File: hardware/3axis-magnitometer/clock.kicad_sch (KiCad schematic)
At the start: 13 parts, among them U1 PCF8563T, Y1 32.768кГц

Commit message: Add files via upload
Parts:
- removed R2, R27, R28, R3: 2.2k, Resistor_SMD:R_0805_2012Metric, symbol Device:R
- removed R4: 10, Resistor_SMD:R_0805_2012Metric, symbol Device:R
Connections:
- net GND: no longer U1.2 (OSCO), Y1.2
- net VCC: now also R1.2
- new net: U1.2 (OSCO), Y1.2
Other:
- moved on the sheet: BT1, C2, C3, D1, R1

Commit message: начата новая трассировка
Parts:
- added C2: 22p, Capacitor_SMD:C_0805_2012Metric, symbol Device:C
- renumbered C2 to C3, C3 to C4
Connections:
- net GND: now also C2.2
- net at U1.2 (OSCO), Y1.2: now also C2.1
- net CLK0: no longer names the net of U1.7 (CLKO)
- net INT: no longer names the net of U1.3 (~{INT})
- no-connect marks 0 -> 2
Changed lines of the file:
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@@
 	(paper "A4")
+	(junction
+		(at 100.33 116.84)
+		(diameter 0)
+		(color 0 0 0 0)
+	)
 	(junction
 		(at 124.46 121.92)
@@
 	)
 	(junction
+		(at 86.36 116.84)
+		(diameter 0)
+		(color 0 0 0 0)
+	)
+	(junction
 		(at 100.33 106.68)
 		(diameter 0)
@@
 		(color 0 0 0 0)
 	)
+	(no_connect
+		(at 147.32 116.84)
+	)
+	(no_connect
+		(at 147.32 114.3)
+	)
 	(wire
 		(pts
@@
 	(wire
 		(pts
+			(xy 86.36 116.84) (xy 86.36 106.68)
+		)
+		(stroke
+			(width 0)
+			(type default)
+		)
+	)
+	(wire
+		(pts
+			(xy 97.79 116.84) (xy 100.33 116.84)
+		)
+		(stroke
+			(width 0)
+			(type default)
+		)
+	)
+	(wire
+		(pts
 			(xy 100.33 115.57) (xy 100.33 116.84)
 		)
@@
 	(wire
 		(pts
-			(xy 86.36 121.92) (xy 86.36 106.68)
+			(xy 86.36 116.84) (xy 90.17 116.84)
+		)
+		(stroke
+			(width 0)
+			(type default)
+		)
+	)
+	(wire
+		(pts
+			(xy 86.36 121.92) (xy 86.36 116.84)
 		)
 		(stroke
@@
 		)
 	)
-	(hierarchical_label "CLK0"
-		(shape output)
-		(at 147.32 114.3 0)
-		(effects
-			(font
-				(size 1.27 1.27)
-			)
-			(justify left)
-		)
-	)
 	(hierarchical_label "SCL"
 		(shape input)
@@
 		)
 	)
-	(hierarchical_label "INT"
-		(shape output)
-		(at 147.32 116.84 0)
-		(effects
-			(font
-				(size 1.27 1.27)
-			)
-			(justify left)
-		)
-	)
 	(hierarchical_label "GND"
 		(shape input)
@@
 			)
 			(justify left)
+		)
+	)
+	(symbol
+		(lib_id "Device:C")
+		(at 93.98 116.84 270)
+		(unit 1)
+		(exclude_from_sim no)
+		(in_bom yes)
+		(on_board yes)
+		(dnp no)
+		(property "Reference" "C2"
+			(at 93.726 110.744 90)
+			(effects
+				(font
+					(size 1.27 1.27)
+				)
+			)
+		)
+		(property "Value" "22p"
+			(at 94.234 112.776 90)
+			(effects
+				(font
+					(size 1.27 1.27)
+				)
+			)
+		)
+		(property "Footprint" "Capacitor_SMD:C_0805_2012Metric"
+			(at 90.17 117.8052 0)
+			(effects
+				(font
+					(size 1.27 1.27)
+				)
+				(hide yes)
+			)
+		)
+		(property "Datasheet" "~"
+			(at 93.98 116.84 0)
+			(effects
+				(font
+					(size 1.27 1.27)
+				)
+				(hide yes)
+			)
+		)
+		(property "Description" "Unpolarized capacitor"
+			(at 93.98 116.84 0)
+			(effects
+				(font
+					(size 1.27 1.27)
+				)
+				(hide yes)
+			)
+		)
+		(pin "1"
+		)
+		(pin "2"
+		)
+		(instances
+			(project "3axis-magnitometer"
+				(path "/c590c88d-27c9-4e5a-a435-a42d9de70c1c/4936c154-a85e-4cc9-be3c-d9a8854356bc"
+					(reference "C2")
+					(unit 1)
+				)
+			)
 		)
 	)
@@
 		(on_board yes)
 		(dnp no)
-		(property "Reference" "C3"
+		(property "Reference" "C4"
 			(at 110.49 92.456 90)
 			(effects
@@
 			(project "3axis-magnitometer"
 				(path "/c590c88d-27c9-4e5a-a435-a42d9de70c1c/4936c154-a85e-4cc9-be3c-d9a8854356bc"
-					(reference "C3")
+					(reference "C4")
 					(unit 1)
 				)
@@
 		(dnp no)
 		(fields_autoplaced yes)
-		(property "Reference" "C2"
+		(property "Reference" "C3"
 			(at 111.379 68.58 90)
 			(effects
@@
 			(project ""
 				(path "/c590c88d-27c9-4e5a-a435-a42d9de70c1c/4936c154-a85e-4cc9-be3c-d9a8854356bc"
-					(reference "C2")
-					(unit 1)
-				)
+					(reference "C3")
+					(unit 1)
+				)

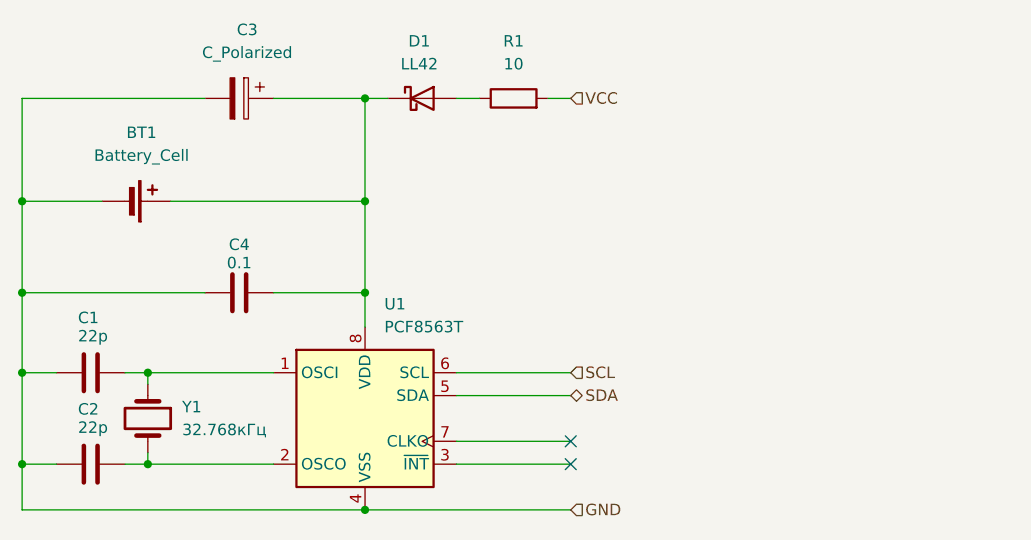
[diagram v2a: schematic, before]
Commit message: Магнитометр правки
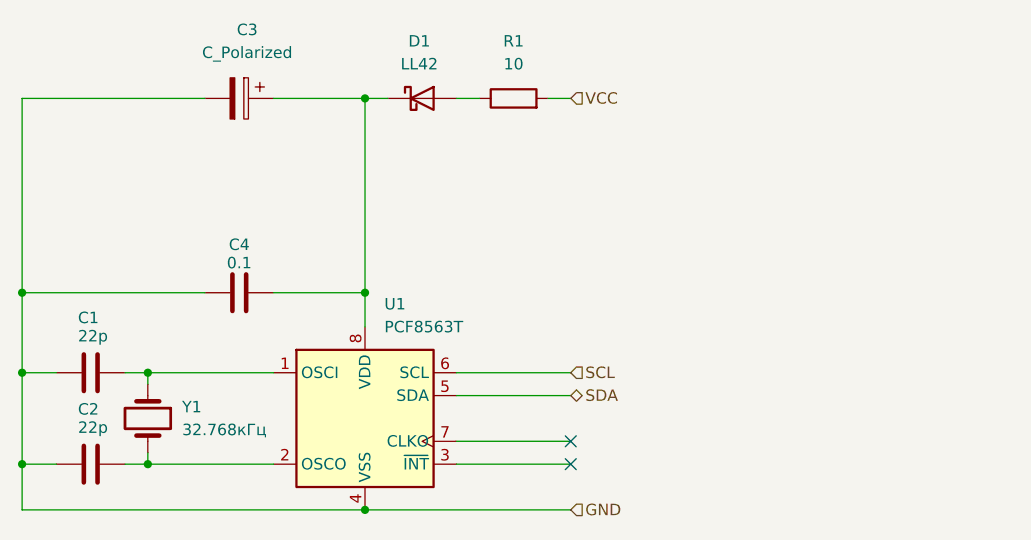
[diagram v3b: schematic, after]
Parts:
- removed BT1: Battery_Cell, Battery:Battery_Panasonic_CR2032-HFN_Horizontal_CircularHoles, symbol Device:Battery_Cell
- C3: footprint Battery:Battery_Panasonic_CR2032-HFN_Horizontal_CircularHoles -> IONISTOR:DSK
- Y1: footprint Crystal:Crystal_SMD_EuroQuartz_EQ161-2Pin_3.2x1.5mm -> Crystal:Crystal_AT310_D3.0mm_L10.0mm_Horizontal_1EP_style2
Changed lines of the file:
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@@
-	)
-	(junction
-		(at 124.46 87.63)
-		(diameter 0)
-		(color 0 0 0 0)
 	)
 	(junction
@@
 	)
 	(junction
-		(at 86.36 87.63)
-		(diameter 0)
-		(color 0 0 0 0)
-	)
-	(junction
 		(at 86.36 106.68)
 		(diameter 0)
@@
 	(wire
 		(pts
-			(xy 86.36 87.63) (xy 86.36 97.79)
+			(xy 86.36 76.2) (xy 86.36 97.79)
 		)
 		(stroke
@@
 	(wire
 		(pts
-			(xy 102.87 87.63) (xy 124.46 87.63)
-		)
-		(stroke
-			(width 0)
-			(type default)
-		)
-	)
-	(wire
-		(pts
 			(xy 124.46 76.2) (xy 127 76.2)
 		)
@@
 	(wire
 		(pts
-			(xy 124.46 76.2) (xy 124.46 87.63)
-		)
-		(stroke
-			(width 0)
-			(type default)
-		)
-	)
-	(wire
-		(pts
 			(xy 144.78 76.2) (xy 147.32 76.2)
 		)
@@
 	(wire
 		(pts
-			(xy 124.46 87.63) (xy 124.46 97.79)
+			(xy 124.46 76.2) (xy 124.46 97.79)
 		)
 		(stroke
@@
 		(pts
 			(xy 134.62 76.2) (xy 137.16 76.2)
-		)
-		(stroke
-			(width 0)
-			(type default)
-		)
-	)
-	(wire
-		(pts
-			(xy 86.36 76.2) (xy 86.36 87.63)
-		)
-		(stroke
-			(width 0)
-			(type default)
-		)
-	)
-	(wire
-		(pts
-			(xy 86.36 87.63) (xy 95.25 87.63)
 		)
 		(stroke
@@
 			)
 		)
-		(property "Footprint" "Crystal:Crystal_SMD_EuroQuartz_EQ161-2Pin_3.2x1.5mm"
+		(property "Footprint" "Crystal:Crystal_AT310_D3.0mm_L10.0mm_Horizontal_1EP_style2"
 			(at 100.33 111.76 0)
 			(effects
@@
 	)
 	(symbol
-		(lib_id "Device:Battery_Cell")
-		(at 97.79 87.63 270)
-		(mirror x)
-		(unit 1)
-		(exclude_from_sim no)
-		(in_bom yes)
-		(on_board yes)
-		(dnp no)
-		(property "Reference" "BT1"
-			(at 99.6315 80.01 90)
-			(effects
-				(font
-					(size 1.27 1.27)
-				)
-			)
-		)
-		(property "Value" "Battery_Cell"
-			(at 99.6315 82.55 90)
-			(effects
-				(font
-					(size 1.27 1.27)
-				)
-			)
-		)
-		(property "Footprint" "Battery:Battery_Panasonic_CR2032-HFN_Horizontal_CircularHoles"
-			(at 99.314 87.63 90)
-			(effects
-				(font
-					(size 1.27 1.27)
-				)
-				(hide yes)
-			)
-		)
-		(property "Datasheet" "~"
-			(at 99.314 87.63 90)
-			(effects
-				(font
-					(size 1.27 1.27)
-				)
-				(hide yes)
-			)
-		)
-		(property "Description" "Single-cell battery"
-			(at 97.79 87.63 0)
-			(effects
-				(font
-					(size 1.27 1.27)
-				)
-				(hide yes)
-			)
-		)
-		(pin "1"
-		)
-		(pin "2"
-		)
-		(instances
-			(project "clock"
-				(path "/051bd5a1-fd18-4bd7-9a14-a1b599706985"
-					(reference "BT?")
-					(unit 1)
-				)
-			)
-			(project ""
-				(path "/c590c88d-27c9-4e5a-a435-a42d9de70c1c/4936c154-a85e-4cc9-be3c-d9a8854356bc"
-					(reference "BT1")
-					(unit 1)
-				)
-			)
-		)
-	)
-	(symbol
 		(lib_id "Device:C_Polarized")
 		(at 110.49 76.2 270)
@@
 			)
 		)
-		(property "Footprint" "Battery:Battery_Panasonic_CR2032-HFN_Horizontal_CircularHoles"
+		(property "Footprint" "IONISTOR:DSK"
 			(at 106.68 77.1652 0)
 			(effects

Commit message: Финальные правки трассировки
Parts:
- added C3: C_Polarized, IONISTOR:DSK, symbol Device:C_Polarized
- renumbered C3 to C4, C4 to C5
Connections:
- net GND: now also C3.2
- net at C4.1, C5.2, D1.1 (K)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: now also C3.1
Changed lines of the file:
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@@
+	)
+	(junction
+		(at 86.36 86.36)
+		(diameter 0)
+		(color 0 0 0 0)
 	)
 	(junction
@@
 	)
 	(junction
+		(at 124.46 86.36)
+		(diameter 0)
+		(color 0 0 0 0)
+	)
+	(junction
 		(at 86.36 97.79)
 		(diameter 0)
@@
 	(wire
 		(pts
-			(xy 86.36 76.2) (xy 86.36 97.79)
+			(xy 86.36 76.2) (xy 86.36 86.36)
 		)
 		(stroke
@@
 	(wire
 		(pts
+			(xy 86.36 86.36) (xy 86.36 97.79)
+		)
+		(stroke
+			(width 0)
+			(type default)
+		)
+	)
+	(wire
+		(pts
 			(xy 114.3 106.68) (xy 100.33 106.68)
 		)
@@
 	(wire
 		(pts
+			(xy 124.46 86.36) (xy 124.46 97.79)
+		)
+		(stroke
+			(width 0)
+			(type default)
+		)
+	)
+	(wire
+		(pts
 			(xy 114.3 97.79) (xy 124.46 97.79)
 		)
@@
 	(wire
 		(pts
+			(xy 107.95 86.36) (xy 124.46 86.36)
+		)
+		(stroke
+			(width 0)
+			(type default)
+		)
+	)
+	(wire
+		(pts
 			(xy 124.46 121.92) (xy 147.32 121.92)
 		)
@@
 	(wire
 		(pts
+			(xy 86.36 86.36) (xy 100.33 86.36)
+		)
+		(stroke
+			(width 0)
+			(type default)
+		)
+	)
+	(wire
+		(pts
 			(xy 144.78 76.2) (xy 147.32 76.2)
 		)
@@
 	(wire
 		(pts
-			(xy 124.46 76.2) (xy 124.46 97.79)
+			(xy 124.46 76.2) (xy 124.46 86.36)
 		)
 		(stroke
@@
 	)
 	(symbol
+		(lib_id "Device:C_Polarized")
+		(at 104.14 86.36 270)
+		(unit 1)
+		(exclude_from_sim no)
+		(in_bom yes)
+		(on_board yes)
+		(dnp no)
+		(fields_autoplaced yes)
+		(property "Reference" "C3"
+			(at 105.029 78.74 90)
+			(effects
+				(font
+					(size 1.27 1.27)
+				)
+			)
+		)
+		(property "Value" "C_Polarized"
+			(at 105.029 81.28 90)
+			(effects
+				(font
+					(size 1.27 1.27)
+				)
+			)
+		)
+		(property "Footprint" "IONISTOR:DSK"
+			(at 100.33 87.3252 0)
+			(effects
+				(font
+					(size 1.27 1.27)
+				)
+				(hide yes)
+			)
+		)
+		(property "Datasheet" "~"
+			(at 104.14 86.36 0)
+			(effects
+				(font
+					(size 1.27 1.27)
+				)
+				(hide yes)
+			)
+		)
+		(property "Description" "Polarized capacitor"
+			(at 104.14 86.36 0)
+			(effects
+				(font
+					(size 1.27 1.27)
+				)
+				(hide yes)
+			)
+		)
+		(pin "2"
+		)
+		(pin "1"
+		)
+		(instances
+			(project "3axis-magnitometer"
+				(path "/c590c88d-27c9-4e5a-a435-a42d9de70c1c/4936c154-a85e-4cc9-be3c-d9a8854356bc"
+					(reference "C3")
+					(unit 1)
+				)
+			)
+		)
+	)
+	(symbol
 		(lib_id "Device:C")
 		(at 110.49 97.79 90)
@@
 		(on_board yes)
 		(dnp no)
-		(property "Reference" "C4"
+		(property "Reference" "C5"
 			(at 110.49 92.456 90)
 			(effects
@@
 			(project "3axis-magnitometer"
 				(path "/c590c88d-27c9-4e5a-a435-a42d9de70c1c/4936c154-a85e-4cc9-be3c-d9a8854356bc"
-					(reference "C4")
+					(reference "C5")
 					(unit 1)
 				)
@@
 		(dnp no)
 		(fields_autoplaced yes)
-		(property "Reference" "C3"
+		(property "Reference" "C4"
 			(at 111.379 68.58 90)
 			(effects
@@
 			(project ""
 				(path "/c590c88d-27c9-4e5a-a435-a42d9de70c1c/4936c154-a85e-4cc9-be3c-d9a8854356bc"
-					(reference "C3")
-					(unit 1)
-				)
+					(reference "C4")
+					(unit 1)
+				)
